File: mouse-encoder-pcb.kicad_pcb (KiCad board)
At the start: 2 copper layers, 16.2 x 12.5 mm, 9 parts, among them SW1 RotaryEncoder, U2 FPC_0_5-8P_HYH2_0

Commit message: working square version
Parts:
- removed U2: FPC_0_5-8P_HYH2_0, MyKicadFootprints:FPC-SMD_8P-P0.50_AFC24-S08FCA-00
- added J1: vik-module-connector, MyKicadFootprints:FPC-SMD_12P-P0.50_HCTL_XW05202-120R-00, F.Cu at (167.1, 81.7)
- added LOGO2: **REF, Vik:vik-logo-small, B.Cu at (163.9, 80.4)
- moved C1 3.28 mm to (169.1, 77.7)
- moved C2 3.05 mm to (164.7, 77.7)
- moved LOGO1 2.25 mm to (172.2, 83.0)
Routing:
- net +3V3: track 3.94 -> 11.2 mm, vias 0 -> 2
- net GND: track 9.91 -> 4.22 mm, vias 4 -> 6
- net Net-(J1-GP_AD2): track 13.0 -> 8.08 mm
- net Net-(J1-GP_AD1): track 10.4 -> 9.14 mm
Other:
- board size 16.2 x 12.5 mm -> 16.5 x 16.5 mm

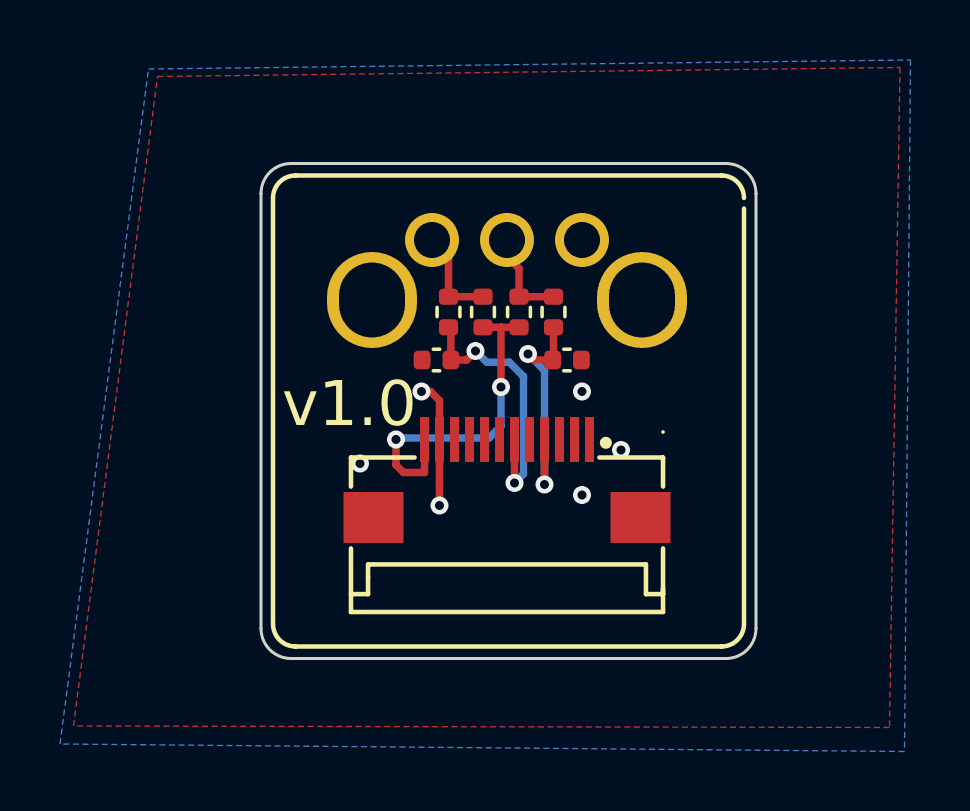
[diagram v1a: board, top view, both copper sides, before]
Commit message: updating footprints
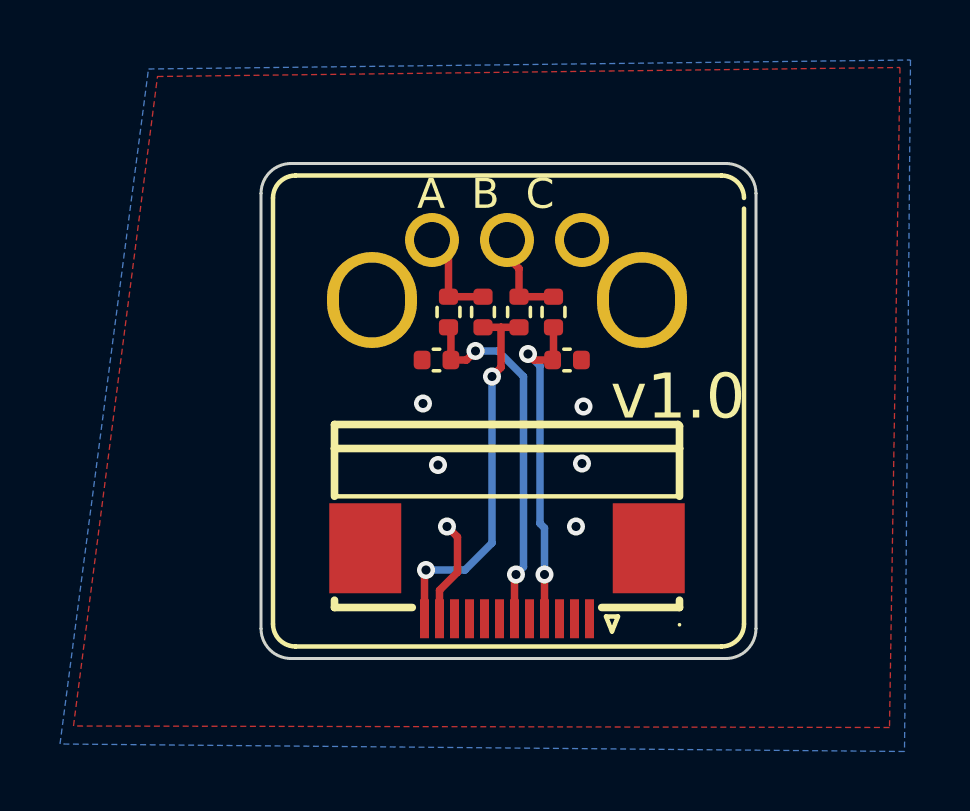
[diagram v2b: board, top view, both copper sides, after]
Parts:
- J1: footprint MyKicadFootprints:FPC-SMD_12P-P0.50_HCTL_XW05202-120R-00 -> MyKicadFootprints:FFC-SMD_FFC05001-12SBA124W5M
- moved J1 3.50 mm to (167.1, 85.2), turned to 180 degrees
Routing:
- net Net-(J1-GP_AD1): track 9.14 -> 12.2 mm
- net Net-(J1-GP_AD2): track 8.08 -> 11.1 mm
- net +3V3: track 11.2 -> 12.7 mm
- net GND: track 4.22 -> 3.47 mm
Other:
- board text added: "A B C"
